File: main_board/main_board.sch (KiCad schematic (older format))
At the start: 132 parts, among them J1 stepper 0, J10 24VDCout5, J11 5VDCout0, J12 5VDCout1, J13 5VDCout2, J14 5VDCout3, J15 5VDCout4, J16 5VDCout5, J17 temp0, J18 temp1, J19 I2C, J2 stepper 1, J20 I2C, J21 I2C, J22 I2C, J23 analogIn0, J24 weightSensor, J25 lightSensor, J26 24VDC_in, J27 24VDC to 5VDC step down, J28 24VDC, J29 24VDC, J3 stepper 2, J30 24VDC, J31 5VDC, J32 5VDC, J33 5VDC, J34 analogIn1, J35 reflectiveSensor, J36 24VDC, J37 24VDC, J38 24VDC, J39 5VDC, J4 stepper 3, J40 5VDC, J41 5VDC, J42 encoder, J5 24VDCout0, J6 24VDCout1, J7 24VDCout2, J8 24VDCout3, J9 24VDCout4, Q1 Q_NMOS_GDS, Q10 BS170, Q11 BS170, Q12 BS170, Q2 Q_NMOS_GDS, Q3 Q_NMOS_GDS, Q4 Q_NMOS_GDS, Q5 Q_NMOS_GDS, Q6 Q_NMOS_GDS, Q7 BS170, Q8 BS170, Q9 BS170, U1 ESP32-DEVKITC-32D, U2 PCA9685PW

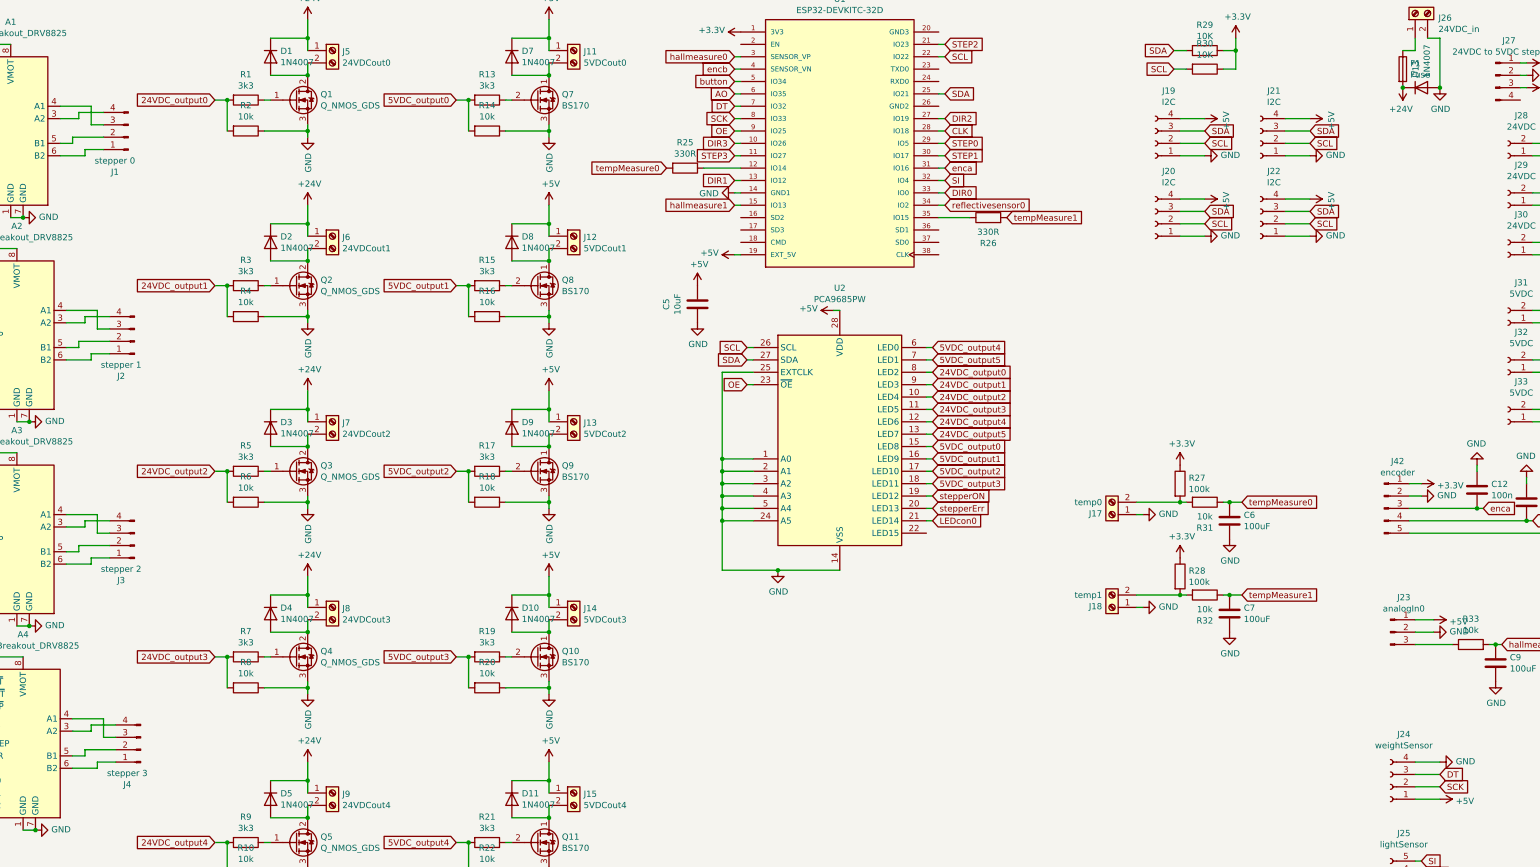
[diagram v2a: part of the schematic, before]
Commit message: GND zones added
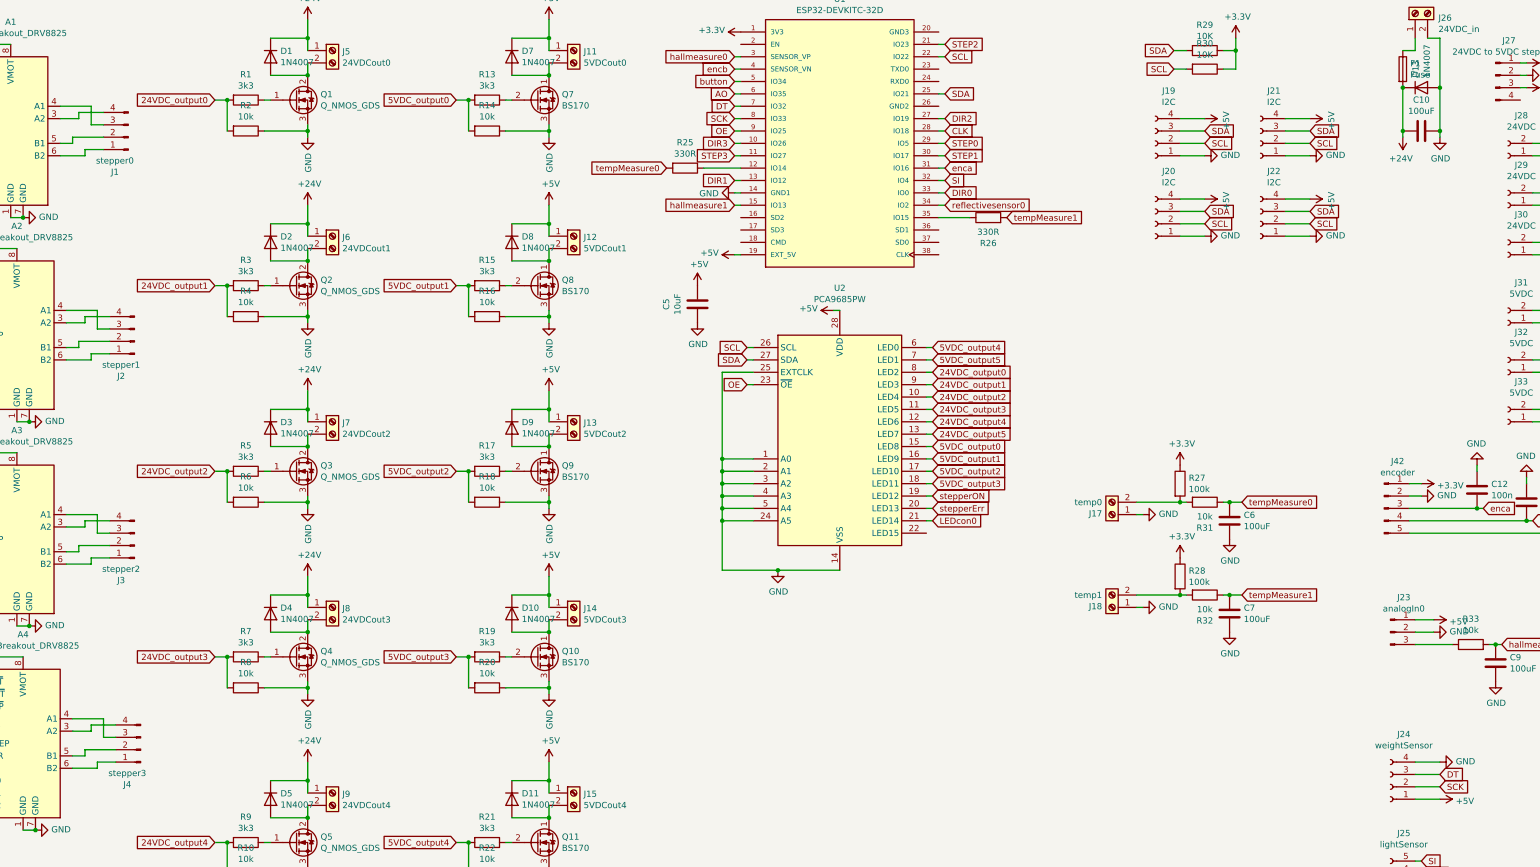
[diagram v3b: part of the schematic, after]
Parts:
- added C10: 100uF, Capacitor_THT:CP_Radial_D6.3mm_P2.50mm, symbol Device:C
- C12, C13, C8: footprint Capacitor_SMD:C_0603_1608Metric_Pad1.08x0.95mm_HandSolder -> Capacitor_SMD:C_1206_3216Metric_Pad1.33x1.80mm_HandSolder
- J1: value stepper 0 -> stepper0
- J2: value stepper 1 -> stepper1
- J3: value stepper 2 -> stepper2
- J4: value stepper 3 -> stepper3
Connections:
- net +24V: now also C10.1
- net GND: now also C10.2
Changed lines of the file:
@@
 L power:+24V #PWR059
 U 1 1 61AAD1AD
-P 13000 1300
-F 0 "#PWR059" H 13000 1150 50  0001 C CNN
-F 1 "+24V" H 13015 1473 50  0000 C CNN
-F 2 "" H 13000 1300 50  0001 C CNN
-F 3 "" H 13000 1300 50  0001 C CNN
-	1    13000 1300
+P 13000 1700
+F 0 "#PWR059" H 13000 1550 50  0001 C CNN
+F 1 "+24V" H 13015 1873 50  0000 C CNN
+F 2 "" H 13000 1700 50  0001 C CNN
+F 3 "" H 13000 1700 50  0001 C CNN
+	1    13000 1700
 	-1   0    0    1
 $EndComp
@@
 L power:GND #PWR064
 U 1 1 61AADA5A
-P 13300 1300
-F 0 "#PWR064" H 13300 1050 50  0001 C CNN
-F 1 "GND" H 13305 1127 50  0000 C CNN
-F 2 "" H 13300 1300 50  0001 C CNN
-F 3 "" H 13300 1300 50  0001 C CNN
-	1    13300 1300
+P 13300 1700
+F 0 "#PWR064" H 13300 1450 50  0001 C CNN
+F 1 "GND" H 13305 1527 50  0000 C CNN
+F 2 "" H 13300 1700 50  0001 C CNN
+F 3 "" H 13300 1700 50  0001 C CNN
+	1    13300 1700
 	1    0    0    -1
 $EndComp
@@
 P 2700 1700
 F 0 "J1" H 2808 1981 50  0000 C CNN
-F 1 "stepper 0" H 2808 1890 50  0000 C CNN
+F 1 "stepper0" H 2808 1890 50  0000 C CNN
 F 2 "Connector_PinHeader_2.54mm:PinHeader_1x04_P2.54mm_Vertical" H 2700 1700 50  0001 C CNN
 F 3 "~" H 2700 1700 50  0001 C CNN
@@
 P 2750 3350
 F 0 "J2" H 2858 3631 50  0000 C CNN
-F 1 "stepper 1" H 2858 3540 50  0000 C CNN
+F 1 "stepper1" H 2858 3540 50  0000 C CNN
 F 2 "Connector_PinHeader_2.54mm:PinHeader_1x04_P2.54mm_Vertical" H 2750 3350 50  0001 C CNN
 F 3 "~" H 2750 3350 50  0001 C CNN
@@
 P 2750 5000
 F 0 "J3" H 2858 5281 50  0000 C CNN
-F 1 "stepper 2" H 2858 5190 50  0000 C CNN
+F 1 "stepper2" H 2858 5190 50  0000 C CNN
 F 2 "Connector_PinHeader_2.54mm:PinHeader_1x04_P2.54mm_Vertical" H 2750 5000 50  0001 C CNN
 F 3 "~" H 2750 5000 50  0001 C CNN
@@
 P 2800 6650
 F 0 "J4" H 2908 6931 50  0000 C CNN
-F 1 "stepper 3" H 2908 6840 50  0000 C CNN
+F 1 "stepper3" H 2908 6840 50  0000 C CNN
 F 2 "Connector_PinHeader_2.54mm:PinHeader_1x04_P2.54mm_Vertical" H 2800 6650 50  0001 C CNN
 F 3 "~" H 2800 6650 50  0001 C CNN
@@
 F 0 "C8" H 14285 4704 50  0000 R CNN
 F 1 "100n" H 14285 4795 50  0000 R CNN
-F 2 "Capacitor_SMD:C_0603_1608Metric_Pad1.08x0.95mm_HandSolder" H 14438 4600 50  0001 C CNN
+F 2 "Capacitor_SMD:C_1206_3216Metric_Pad1.33x1.80mm_HandSolder" H 14438 4600 50  0001 C CNN
 F 3 "~" H 14400 4750 50  0001 C CNN
 	1    14400 4750
@@
 F 0 "C13" H 13885 4604 50  0000 R CNN
 F 1 "100n" H 13885 4695 50  0000 R CNN
-F 2 "Capacitor_SMD:C_0603_1608Metric_Pad1.08x0.95mm_HandSolder" H 14038 4500 50  0001 C CNN
+F 2 "Capacitor_SMD:C_1206_3216Metric_Pad1.33x1.80mm_HandSolder" H 14038 4500 50  0001 C CNN
 F 3 "~" H 14000 4650 50  0001 C CNN
 	1    14000 4650
@@
 F 0 "C12" H 13485 4504 50  0000 R CNN
 F 1 "100n" H 13485 4595 50  0000 R CNN
-F 2 "Capacitor_SMD:C_0603_1608Metric_Pad1.08x0.95mm_HandSolder" H 13638 4400 50  0001 C CNN
+F 2 "Capacitor_SMD:C_1206_3216Metric_Pad1.33x1.80mm_HandSolder" H 13638 4400 50  0001 C CNN
 F 3 "~" H 13600 4550 50  0001 C CNN
 	1    13600 4550
@@
 	1    0    0    -1
 $EndComp
-Connection ~ 13000 1300
 Wire Wire Line
 	13000 1000 13100 1000
@@
 	14400 4600 14400 4550
 $Comp
-L power:GND #PWR?
+L power:GND #PWR0111
 U 1 1 6212881C
 P 14000 4450
-F 0 "#PWR?" H 14000 4200 50  0001 C CNN
+F 0 "#PWR0111" H 14000 4200 50  0001 C CNN
 F 1 "GND" H 14005 4277 50  0000 C CNN
 F 2 "" H 14000 4450 50  0001 C CNN
@@
 	-1   0    0    1
 $EndComp
+$Comp
+L Device:C C10
+U 1 1 6231B719
+P 13150 1650
+F 0 "C10" V 13402 1650 50  0000 C CNN
+F 1 "100uF" V 13311 1650 50  0000 C CNN
+F 2 "Capacitor_THT:CP_Radial_D6.3mm_P2.50mm" H 13188 1500 50  0001 C CNN
+F 3 "~" H 13150 1650 50  0001 C CNN
+	1    13150 1650
+	0    -1   -1   0
+$EndComp
+Wire Wire Line
+	13300 1300 13300 1650
+Wire Wire Line
+	13300 1700 13300 1650
+Connection ~ 13300 1650
+Wire Wire Line
+	13000 1700 13000 1650
+Wire Wire Line
+	13000 1650 13000 1300
+Connection ~ 13000 1650
+Connection ~ 13000 1300
 $EndSCHEMATC

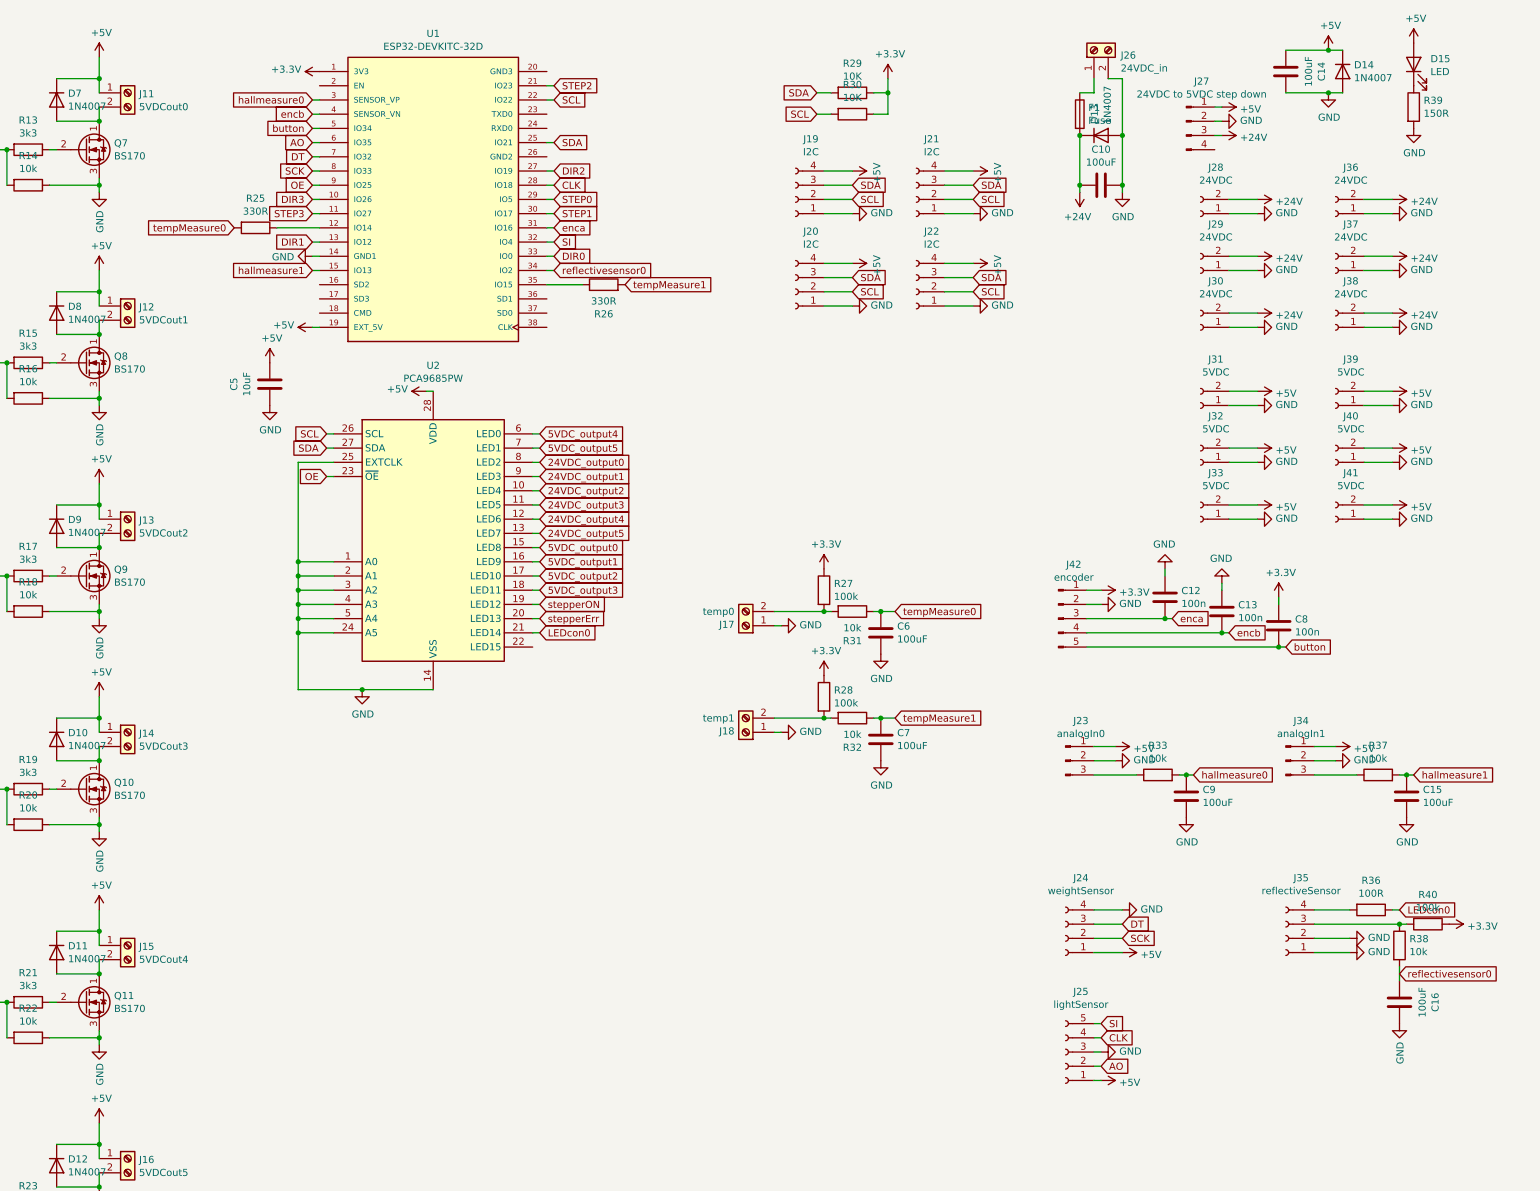
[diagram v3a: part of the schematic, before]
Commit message: ADC 2 unused
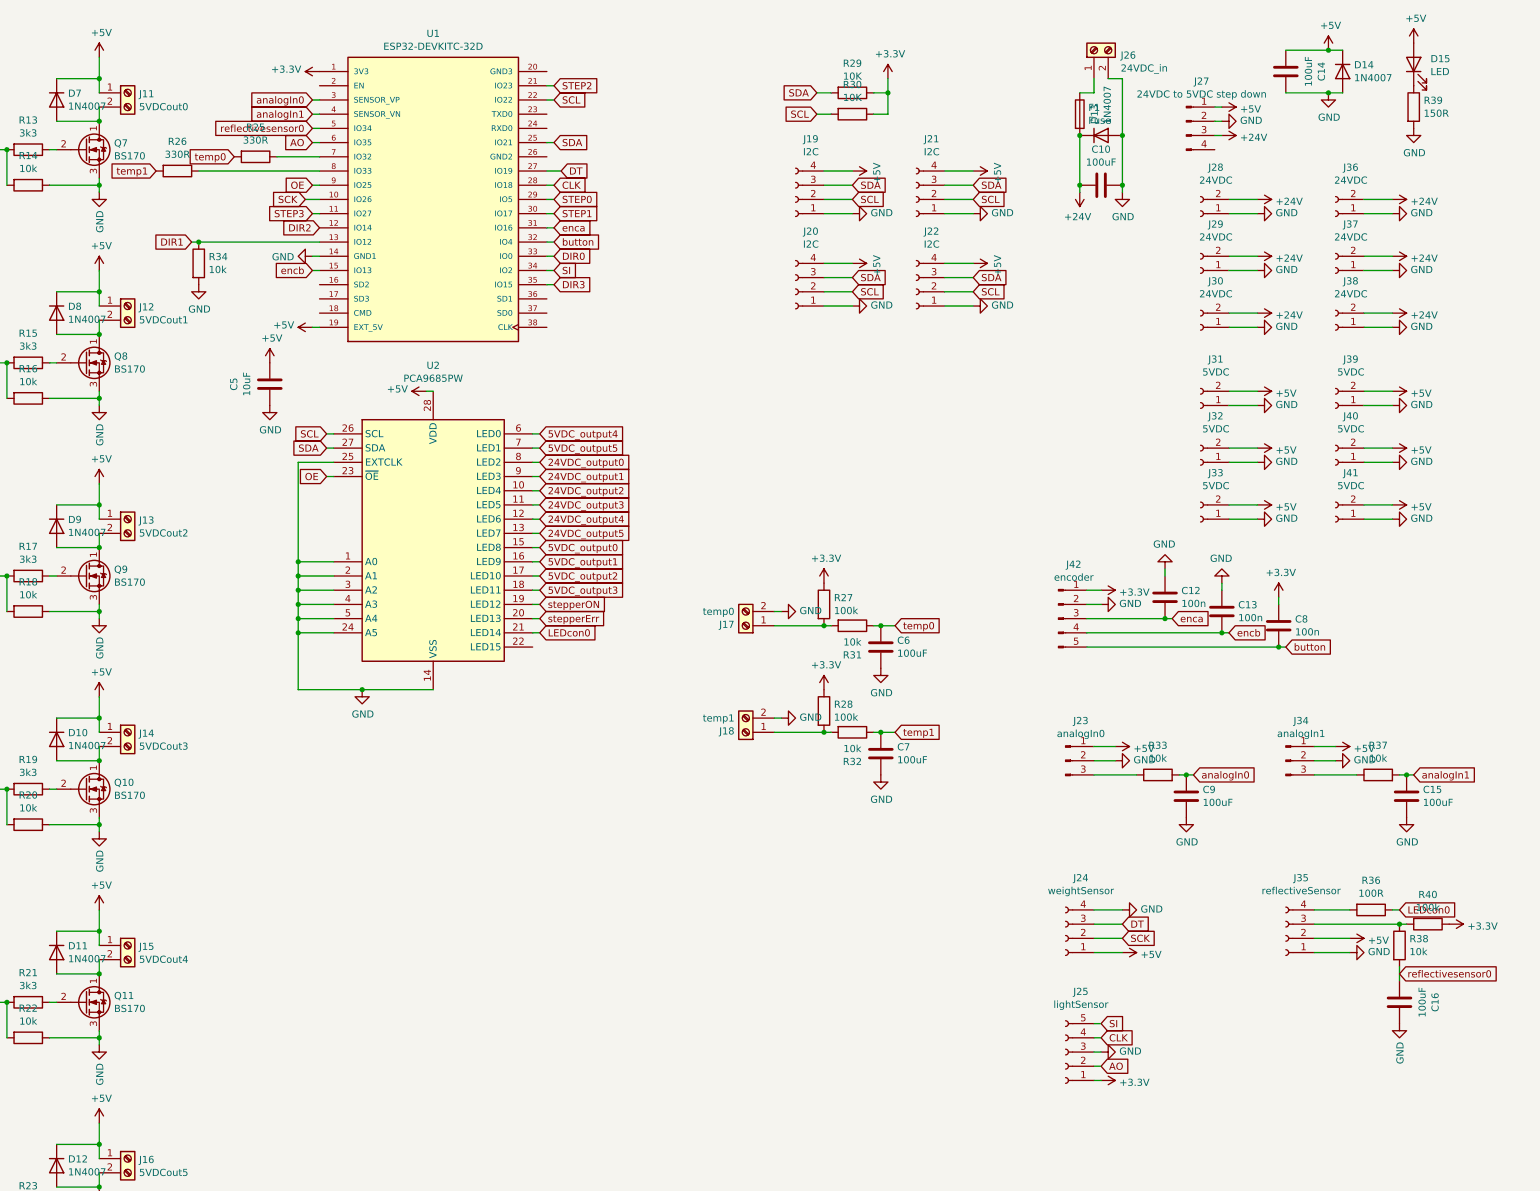
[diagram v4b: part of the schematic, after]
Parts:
- added R34: 10k, Resistor_SMD:R_1206_3216Metric_Pad1.30x1.75mm_HandSolder, symbol Device:R
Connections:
- net +3V3: now also J25.1 (Pin_1)
- net +5V: now also J35.2 (Pin_2); no longer J25.1 (Pin_1)
- net DIR1: now also R34.1
- net DIR2: now also U1.12 (IO14); no longer U1.27 (IO19)
- net DIR3: now also U1.35 (IO15); no longer U1.10 (IO26)
- net DT: now also U1.27 (IO19); no longer U1.7 (IO32)
- net GND: now also J17.2 (Pin_2), J18.2 (Pin_2), R34.2; no longer J17.1 (Pin_1), J18.1 (Pin_1), J35.2 (Pin_2)
- net SCK: now also U1.10 (IO26); no longer U1.8 (IO33)
- net SI: now also U1.34 (IO2); no longer U1.32 (IO4)
- net button: now also U1.32 (IO4); no longer U1.5 (IO34)
- net encb: now also U1.15 (IO13); no longer U1.4 (SENSOR_VN)
- net reflectivesensor0: now also U1.5 (IO34); no longer U1.34 (IO2)
- net at R27.2, R31.2: now also J17.1 (Pin_1); no longer J17.2 (Pin_2)
- net at R25.1: now also U1.7 (IO32); no longer U1.12 (IO14)
- net at R26.1: now also U1.8 (IO33); no longer U1.35 (IO15)
- net at R28.2, R32.2: now also J18.1 (Pin_1); no longer J18.2 (Pin_2)
- net hallmeasure0 renamed analogIn0
- net hallmeasure1 renamed analogIn1
- net analogIn1: now also U1.4 (SENSOR_VN); no longer U1.15 (IO13)
- net tempMeasure0 renamed temp0
- net tempMeasure1 renamed temp1
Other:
- moved on the sheet: C6, C7, R25, R26, R27, R28, R31, R32

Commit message: problems fix
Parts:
- removed C10, C14, C15, C16, C6, C7, C9: 100uF, Capacitor_THT:CP_Radial_D6.3mm_P2.50mm, symbol Device:C
- removed C5: 10uF, Capacitor_THT:CP_Radial_D4.0mm_P1.50mm, symbol Device:C
- removed J23: analogIn0, Connector_PinHeader_2.54mm:PinHeader_1x03_P2.54mm_Vertical, symbol Connector:Conn_01x03_Male
- removed J34: analogIn1, Connector_PinHeader_2.54mm:PinHeader_1x03_P2.54mm_Vertical, symbol Connector:Conn_01x03_Male
- added C10, C14, C15, C16, C6, C7, C9: 100uF, Capacitor_THT:CP_Radial_D6.3mm_P2.50mm, symbol Device:CP
- added C5: 10uF, Capacitor_THT:CP_Radial_D6.3mm_P2.50mm, symbol Device:CP
- added D16: LED, LED_THT:LED_D3.0mm, symbol Device:LED
- added J23: analogIn0, Connector_PinHeader_2.54mm:PinHeader_1x04_P2.54mm_Vertical, symbol Connector:Conn_01x04_Male
- added J34: analogIn1, Connector_PinHeader_2.54mm:PinHeader_1x04_P2.54mm_Vertical, symbol Connector:Conn_01x04_Male
- added R35: R, Resistor_SMD:R_1206_3216Metric_Pad1.30x1.75mm_HandSolder, symbol Device:R
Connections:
- net +24V: now also C10.1
- net +3V3: now also J24.1 (Pin_1), J23.1 (Pin_1), J34.1 (Pin_1)
- net +5V: now also C14.1, C5.1, J23.2 (Pin_2), J34.2 (Pin_2), R35.1; no longer J24.1 (Pin_1)
- net DIR0: now also U1.29 (IO5); no longer U1.33 (IO0)
- net GND: now also U1.20 (GND3), U1.26 (GND2), C10.2, C14.2, C15.2, C16.2, C5.2, C6.2, C7.2, C9.2, J23.3 (Pin_3), J34.3 (Pin_3)
- net STEP0: now also U1.33 (IO0); no longer U1.29 (IO5)
- net reflectivesensor0: no longer R38.2
- net temp0: now also C6.1
- net temp1: now also C7.1
- net at U2.22 (LED15): now also D16.1 (K)
- net at R37.1: now also J34.4 (Pin_4)
- net at R33.1: now also J23.4 (Pin_4)
- new net: D16.2 (A), R35.2
- new net reflectiveSensor0: C16.1, R38.2
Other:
- moved on the sheet: R34

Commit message: reflectiveSensor
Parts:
- removed R25, R26: 330R, Resistor_SMD:R_1206_3216Metric_Pad1.30x1.75mm_HandSolder, symbol Device:R
- D15: value LED -> powerOn
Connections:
- net reflectivesensor0 is gone; now on net reflectiveSensor0: U1.5 (IO34)
- net DIR1: now also U1.33 (IO0); no longer R34.1, U1.13 (IO12)
- net STEP0: now also R34.1, U1.13 (IO12); no longer U1.33 (IO0)
- net temp0: now also U1.7 (IO32)
- net temp1: now also U1.8 (IO33)
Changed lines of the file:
@@
 STEP3
 Text GLabel 7600 1250 0    50   Input ~ 0
-reflectivesensor0
+reflectiveSensor0
 Text GLabel 7550 1750 0    50   Input ~ 0
 SCK
@@
 	0    1    1    0
 $EndComp
-$Comp
-L Device:R R25
-U 1 1 6025E97A
-P 7200 1450
-F 0 "R25" V 6993 1450 50  0000 C CNN
-F 1 "330R" V 7084 1450 50  0000 C CNN
-F 2 "Resistor_SMD:R_1206_3216Metric_Pad1.30x1.75mm_HandSolder" V 7130 1450 50  0001 C CNN
-F 3 "~" H 7200 1450 50  0001 C CNN
-	1    7200 1450
-	0    1    1    0
-$EndComp
-$Comp
-L Device:R R26
-U 1 1 6025F50D
-P 6650 1550
-F 0 "R26" V 6443 1550 50  0000 C CNN
-F 1 "330R" V 6534 1550 50  0000 C CNN
-F 2 "Resistor_SMD:R_1206_3216Metric_Pad1.30x1.75mm_HandSolder" V 6580 1550 50  0001 C CNN
-F 3 "~" H 6650 1550 50  0001 C CNN
-	1    6650 1550
-	0    1    1    0
-$EndComp
-Text GLabel 7050 1450 0    50   Input ~ 0
+Text GLabel 7600 1450 0    50   Input ~ 0
 temp0
-Text GLabel 6500 1550 0    50   Input ~ 0
+Text GLabel 7600 1550 0    50   Input ~ 0
 temp1
 $Comp
@@
 Text GLabel 9300 1950 2    50   Input ~ 0
 enca
-Text GLabel 7050 2050 0    50   Input ~ 0
+Text GLabel 9300 2150 2    50   Input ~ 0
 DIR1
 Text GLabel 9300 1850 2    50   Input ~ 0
@@
 Text GLabel 9300 1750 2    50   Input ~ 0
 DIR0
-Text GLabel 9300 2150 2    50   Input ~ 0
+Text GLabel 7050 2050 0    50   Input ~ 0
 STEP0
 $Comp
@@
 P 15350 800
 F 0 "D15" V 15389 682 50  0000 R CNN
-F 1 "LED" V 15298 682 50  0000 R CNN
+F 1 "powerOn" V 15298 682 50  0000 R CNN
 F 2 "LED_THT:LED_D3.0mm" H 15350 800 50  0001 C CNN
 F 3 "~" H 15350 800 50  0001 C CNN
@@
 $EndComp
 Wire Wire Line
-	7350 1450 7650 1450
-Wire Wire Line
 	7600 1050 7650 1050
 Wire Wire Line
@@
 Wire Wire Line
 	7600 1150 7650 1150
-Wire Wire Line
-	6800 1550 7650 1550
 Wire Wire Line
 	9250 2250 9300 2250
@@
 Wire Wire Line
 	14800 5500 14650 5500
+Wire Wire Line
+	7600 1450 7650 1450
+Wire Wire Line
+	7600 1550 7650 1550
 $EndSCHEMATC
